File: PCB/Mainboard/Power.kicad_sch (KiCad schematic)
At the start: 17 parts, among them Q1 P-Channel, U4 TPS62177, U5 TPS2111

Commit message: Update schematic and lay-out
- Swap out CP2102N, ATmega328PB and CP with new Kicad 6 symbol
- Correct all links to point to new zoudio_symbols and zoudio_footprint libraries
- Lay-out updated, only antenna is left to update.
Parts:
- Q1: footprint ZOUDIO-footprints:SOIC8_mosfet -> zoudio_footprints:SOIC8_mosfet
- U4: footprint ZOUDIO-footprints:WSON-10-1EP_2x3mm_P0.5mm_EP0.84x2.4mm -> zoudio_footprints:WSON-10-1EP_2x3mm_P0.5mm_EP0.84x2.4mm
- U5: symbol ZOUDIO-symbols:TPS211xA -> zoudio_symbols:TPS211xA
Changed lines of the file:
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@@
       (effects (font (size 1.524 1.524)))
     )
-    (property "Footprint" "ZOUDIO-footprints:SOIC8_mosfet" (id 2) (at 87.63 128.27 0)
+    (property "Footprint" "zoudio_footprints:SOIC8_mosfet" (id 2) (at 87.63 128.27 0)
       (effects (font (size 1.524 1.524)) hide)
     )
@@
     (property "Reference" "U4" (id 0) (at 107.95 73.66 0))
     (property "Value" "TPS62177" (id 1) (at 107.95 76.2 0))
-    (property "Footprint" "ZOUDIO-footprints:WSON-10-1EP_2x3mm_P0.5mm_EP0.84x2.4mm" (id 2) (at 111.76 100.33 0)
+    (property "Footprint" "zoudio_footprints:WSON-10-1EP_2x3mm_P0.5mm_EP0.84x2.4mm" (id 2) (at 111.76 100.33 0)
       (effects (font (size 1.27 1.27)) (justify left) hide)
     )
@@
     (pin "1")
   )
-  (symbol (lib_id "ZOUDIO-symbols:TPS211xA") (at 196.85 88.9 0) (unit 1)
+  (symbol (lib_id "zoudio_symbols:TPS211xA") (at 196.85 88.9 0) (unit 1)
     (in_bom yes) (on_board yes)
     (property "Reference" "U5" (id 0) (at 196.85 81.28 0))

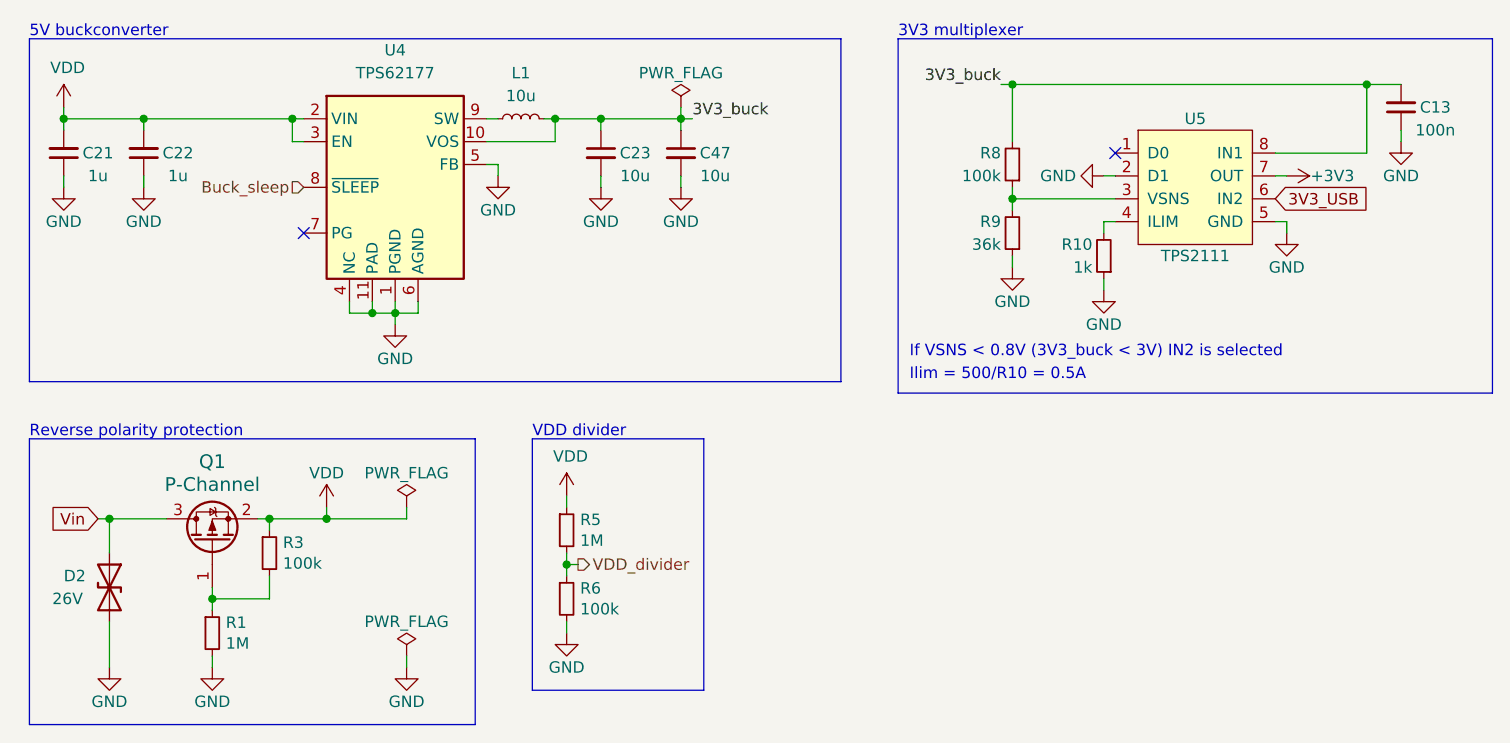
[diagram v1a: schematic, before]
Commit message: Add buck, change some part values
Add new buck in schematic and layout.
Modify BT module footprint,
Change power led resistor from 1k to 100R
Change 4.7u TAS resistors to 10u (consolidation)
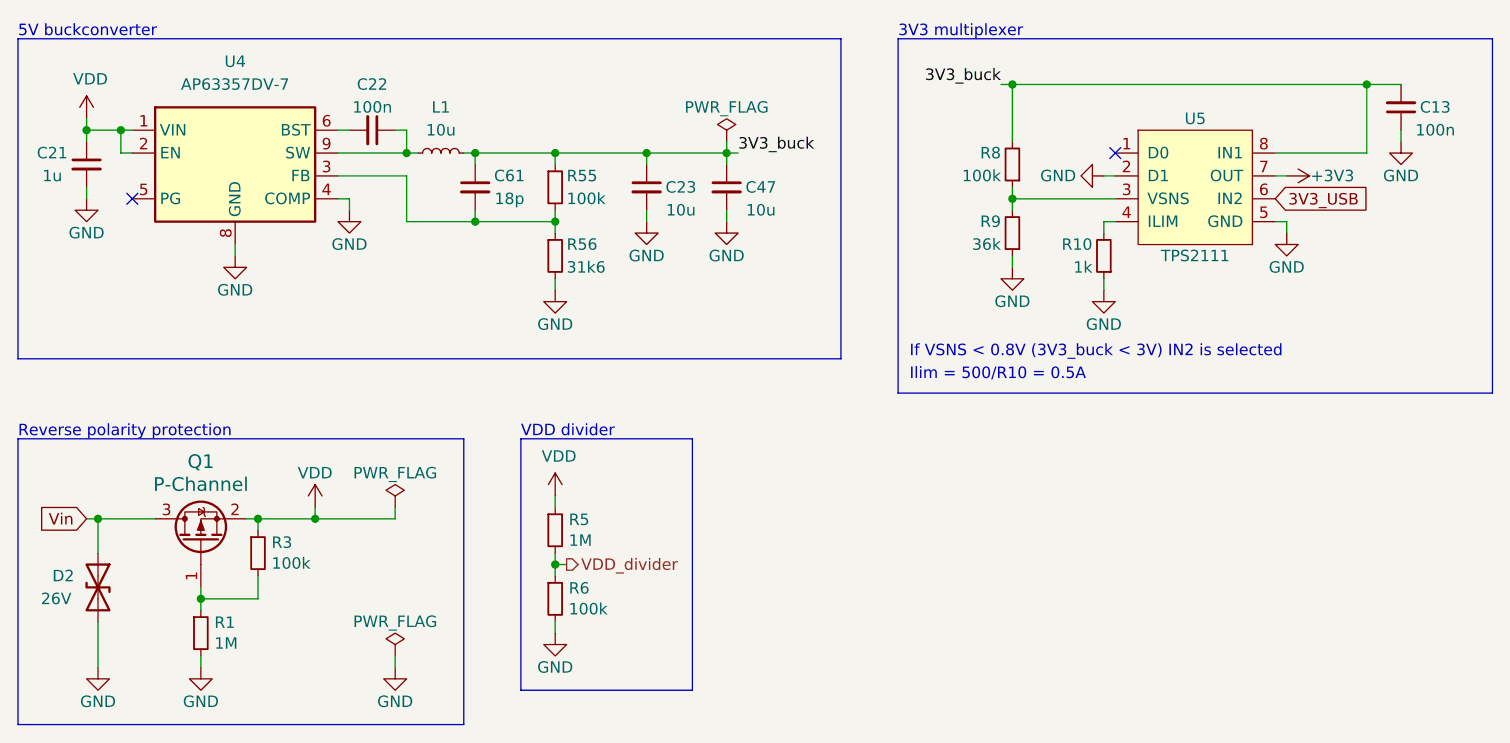
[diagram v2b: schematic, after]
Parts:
- removed U4: TPS62177, zoudio_footprints:WSON-10-1EP_2x3mm_P0.5mm_EP0.84x2.4mm, symbol Regulator_Switching:TPS62177DQC
- added C61: 18p, Capacitor_SMD:C_0603_1608Metric, symbol Device:C_Small
- added R55: 100k, Resistor_SMD:R_0603_1608Metric, symbol Device:R_Small
- added R56: 31k6, Resistor_SMD:R_0603_1608Metric, symbol Device:R_Small
- added U4: AP63357DV-7, zoudio_footprints:V-DFN3020-13, symbol zoudio_symbols:AP63357DV-7
- C22: value 1u -> 100n; footprint Capacitor_SMD:C_0805_2012Metric -> Capacitor_SMD:C_0603_1608Metric; Manufacturer Taiyo Yuden -> Murata; Partnumber UMK212B7105KG-T -> GCM188L81H104KA57D
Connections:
- net 3V3_buck: now also C61.1, R55.1
- net GND: now also C21.2, R56.2, U4.4 (COMP), U4.8 (GND); no longer C21.1, C22.1
- net VDD: now also C21.1, U4.1 (VIN), U4.2 (EN); no longer C21.2, C22.2
- net at L1.1: now also C22.1, U4.9 (SW)
- new net: C61.2, R55.2, R56.1, U4.3 (FB)
- new net: C22.2, U4.6 (BST)
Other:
- moved on the sheet: C23, C47, D2, L1, Q1, R1, R3, R5, R6

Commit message: Mainboard: update symbol fields for bom export
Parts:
- C61: Partnumber 0603B104J500CT -> C0603C180K8GACTU
- R55: Partnumber RC0603FR-071KL -> RC0603FR-07100KL
- R56: Partnumber RC0603FR-071KL -> RC0603FR-0731K6L
- U4: Manufacturer (none) -> Diodes Inc; Partnumber (none) -> AP63357DV-7
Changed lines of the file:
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@@
       (effects (font (size 1.27 1.27)) hide)
     )
-    (property "Partnumber" "RC0603FR-071KL" (id 5) (at 125.73 96.52 0)
+    (property "Partnumber" "RC0603FR-0731K6L" (id 5) (at 125.73 96.52 0)
       (effects (font (size 1.27 1.27)) hide)
     )
@@
     )
     (property "Datasheet" "" (id 3) (at 90.17 73.66 0)
+      (effects (font (size 1.27 1.27)) hide)
+    )
+    (property "Manufacturer" "Diodes Inc" (id 4) (at 90.17 87.63 0)
+      (effects (font (size 1.27 1.27)) hide)
+    )
+    (property "Partnumber" "AP63357DV-7" (id 5) (at 90.17 87.63 0)
       (effects (font (size 1.27 1.27)) hide)
     )
@@
       (effects (font (size 1.27 1.27)) hide)
     )
-    (property "Partnumber" "RC0603FR-071KL" (id 5) (at 125.73 88.9 0)
+    (property "Partnumber" "RC0603FR-07100KL" (id 5) (at 125.73 88.9 0)
       (effects (font (size 1.27 1.27)) hide)
     )
@@
       (effects (font (size 1.27 1.27)) hide)
     )
-    (property "Partnumber" "0603B104J500CT" (id 5) (at 116.84 88.9 0)
+    (property "Partnumber" "C0603C180K8GACTU" (id 5) (at 116.84 88.9 0)
       (effects (font (size 1.27 1.27)) hide)
     )

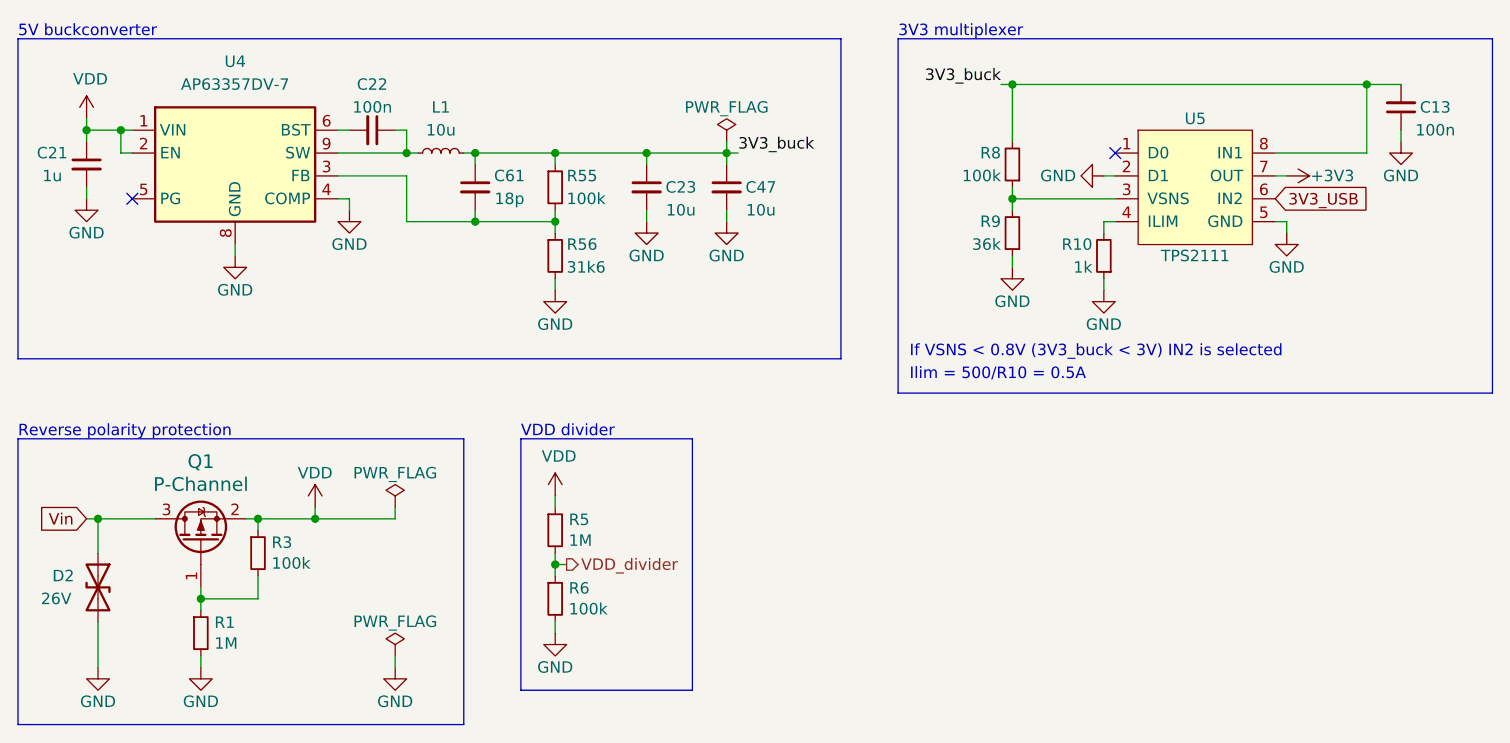
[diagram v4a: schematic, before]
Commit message: Mainboard: version 1.1.1
- No change in electrical connectivity
- Make 3D model more complete
- Improvements in paste layer for manufacturability
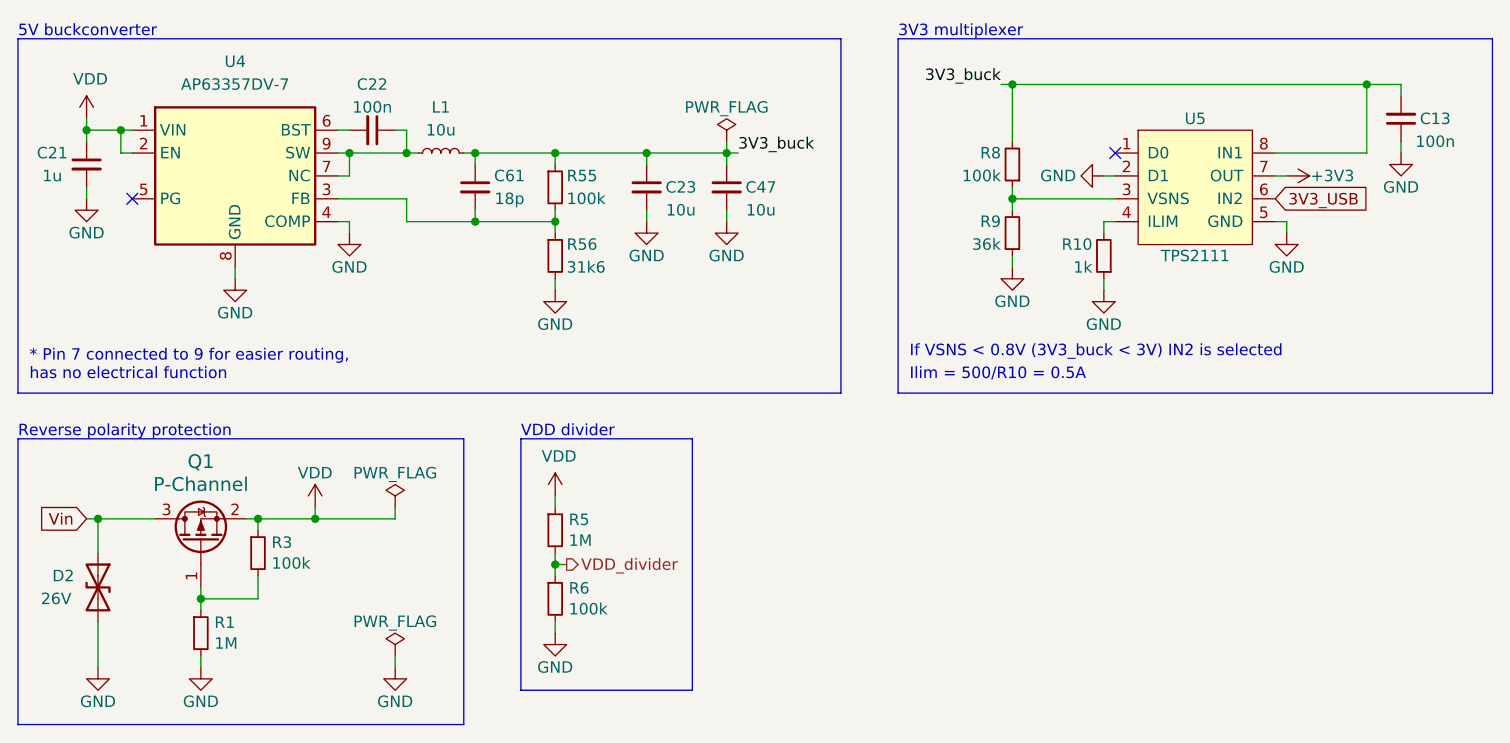
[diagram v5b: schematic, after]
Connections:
- net at C22.1, L1.1, U4.9 (SW): now also U4.7 (NC)
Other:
- note added: "* Pin 7 connected to 9 for easier routing, has no electrical function"
- moved on the sheet: C13
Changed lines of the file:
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@@
   (title_block
     (title "4x38W amp with DSP and BT")
-    (date "2022-02-12")
-    (rev "1.1")
+    (date "2022-04-17")
+    (rev "1.1.1")
     (company "ZOUDIO")
   )
@@
   )
   (junction (at 144.78 85.09) (diameter 0) (color 0 0 0 0)
+  )
+  (junction (at 102.87 85.09) (diameter 0) (color 0 0 0 0)
   )
   (junction (at 215.9 77.47) (diameter 0) (color 0 0 0 0)
@@
     (stroke (width 0) (type default) (color 0 0 0 0))
   )
+  (wire (pts (xy 102.87 87.63) (xy 102.87 85.09))
+    (stroke (width 0) (type default) (color 0 0 0 0))
+  )
   (wire (pts (xy 186.69 93.98) (xy 186.69 92.71))
     (stroke (width 0) (type default) (color 0 0 0 0))
@@
     (stroke (width 0) (type default) (color 0 0 0 0))
   )
+  (wire (pts (xy 101.6 87.63) (xy 102.87 87.63))
+    (stroke (width 0) (type default) (color 0 0 0 0))
+  )
   (wire (pts (xy 186.69 87.63) (xy 187.96 87.63))
     (stroke (width 0) (type default) (color 0 0 0 0))
@@
     (stroke (width 0) (type default) (color 0 0 0 0))
   )
-  (wire (pts (xy 109.22 87.63) (xy 109.22 92.71))
-    (stroke (width 0) (type default) (color 0 0 0 0))
-  )
   (wire (pts (xy 107.95 82.55) (xy 109.22 82.55))
     (stroke (width 0) (type default) (color 0 0 0 0))
@@
     (stroke (width 0) (type default) (color 0 0 0 0))
   )
-  (polyline (pts (xy 157.48 72.39) (xy 157.48 107.95))
+  (polyline (pts (xy 157.48 72.39) (xy 157.48 111.76))
+    (stroke (width 0) (type default) (color 0 0 0 0))
+  )
+  (wire (pts (xy 101.6 90.17) (xy 109.22 90.17))
     (stroke (width 0) (type default) (color 0 0 0 0))
   )
@@
     (stroke (width 0) (type default) (color 0 0 0 0))
   )
+  (wire (pts (xy 219.71 77.47) (xy 219.71 78.74))
+    (stroke (width 0) (type default) (color 0 0 0 0))
+  )
   (wire (pts (xy 77.47 82.55) (xy 77.47 85.09))
     (stroke (width 0) (type default) (color 0 0 0 0))
@@
     (stroke (width 0) (type default) (color 0 0 0 0))
   )
-  (polyline (pts (xy 157.48 107.95) (xy 66.04 107.95))
+  (polyline (pts (xy 157.48 111.76) (xy 66.04 111.76))
     (stroke (width 0) (type default) (color 0 0 0 0))
   )
@@
     (stroke (width 0) (type default) (color 0 0 0 0))
   )
-  (wire (pts (xy 102.87 90.17) (xy 101.6 90.17))
+  (wire (pts (xy 102.87 92.71) (xy 101.6 92.71))
     (stroke (width 0) (type default) (color 0 0 0 0))
   )
@@
     (stroke (width 0) (type default) (color 0 0 0 0))
   )
-  (wire (pts (xy 219.71 82.55) (xy 219.71 83.82))
+  (wire (pts (xy 219.71 83.82) (xy 219.71 85.09))
     (stroke (width 0) (type default) (color 0 0 0 0))
   )
@@
     (stroke (width 0) (type default) (color 0 0 0 0))
   )
-  (wire (pts (xy 90.17 95.25) (xy 90.17 96.52))
+  (wire (pts (xy 90.17 97.79) (xy 90.17 99.06))
     (stroke (width 0) (type default) (color 0 0 0 0))
   )
@@
     (stroke (width 0) (type default) (color 0 0 0 0))
   )
+  (wire (pts (xy 102.87 85.09) (xy 101.6 85.09))
+    (stroke (width 0) (type default) (color 0 0 0 0))
+  )
   (wire (pts (xy 116.84 86.36) (xy 116.84 85.09))
     (stroke (width 0) (type default) (color 0 0 0 0))
@@
     (stroke (width 0) (type default) (color 0 0 0 0))
   )
+  (wire (pts (xy 109.22 90.17) (xy 109.22 92.71))
+    (stroke (width 0) (type default) (color 0 0 0 0))
+  )
   (polyline (pts (xy 229.87 72.39) (xy 229.87 111.76))
     (stroke (width 0) (type default) (color 0 0 0 0))
@@
     (stroke (width 0) (type default) (color 0 0 0 0))
   )
-  (wire (pts (xy 109.22 85.09) (xy 101.6 85.09))
+  (wire (pts (xy 109.22 85.09) (xy 102.87 85.09))
     (stroke (width 0) (type default) (color 0 0 0 0))
   )
@@
     (stroke (width 0) (type default) (color 0 0 0 0))
   )
-  (wire (pts (xy 102.87 91.44) (xy 102.87 90.17))
+  (wire (pts (xy 102.87 93.98) (xy 102.87 92.71))
     (stroke (width 0) (type default) (color 0 0 0 0))
   )
@@
     (stroke (width 0) (type default) (color 0 0 0 0))
   )
-  (polyline (pts (xy 66.04 72.39) (xy 66.04 107.95))
+  (polyline (pts (xy 66.04 72.39) (xy 66.04 111.76))
     (stroke (width 0) (type default) (color 0 0 0 0))
   )
@@
   )
   (polyline (pts (xy 121.92 144.78) (xy 140.97 144.78))
-    (stroke (width 0) (type default) (color 0 0 0 0))
-  )
-  (wire (pts (xy 101.6 87.63) (xy 109.22 87.63))
     (stroke (width 0) (type default) (color 0 0 0 0))
   )
@@
   )
   (text "If VSNS < 0.8V (3V3_buck < 3V) IN2 is selected" (at 165.1 107.95 0)
+    (effects (font (size 1.27 1.27)) (justify left bottom))
+  )
+  (text "* Pin 7 connected to 9 for easier routing, \nhas no electrical function"
+    (at 67.31 110.49 0)
     (effects (font (size 1.27 1.27)) (justify left bottom))
   )
@@
     (pin "1")
   )
-  (symbol (lib_id "Device:C_Small") (at 219.71 80.01 180) (unit 1)
-    (in_bom yes) (on_board yes)
-    (property "Reference" "C13" (id 0) (at 223.52 80.01 0))
-    (property "Value" "100n" (id 1) (at 223.52 82.55 0))
-    (property "Footprint" "Capacitor_SMD:C_0603_1608Metric" (id 2) (at 219.71 80.01 0)
-      (effects (font (size 1.27 1.27)) hide)
-    )
-    (property "Datasheet" "~" (id 3) (at 219.71 80.01 0)
-      (effects (font (size 1.27 1.27)) hide)
-    )
-    (property "Manufacturer" "Murata" (id 4) (at 219.71 80.01 0)
-      (effects (font (size 1.27 1.27)) hide)
-    )
-    (property "Partnumber" "GCM188L81H104KA57D" (id 5) (at 219.71 80.01 0)
-      (effects (font (size 1.27 1.27)) hide)
-    )
-    (pin "1")
-    (pin "2")
-  )
-  (symbol (lib_id "power:GND") (at 219.71 83.82 0) (unit 1)
-    (in_bom yes) (on_board yes)
-    (property "Reference" "#PWR0139" (id 0) (at 219.71 90.17 0)
-      (effects (font (size 1.27 1.27)) hide)
-    )
-    (property "Value" "GND" (id 1) (at 219.71 87.63 0))
-    (property "Footprint" "" (id 2) (at 219.71 83.82 0)
-      (effects (font (size 1.27 1.27)) hide)
-    )
-    (property "Datasheet" "" (id 3) (at 219.71 83.82 0)
+  (symbol (lib_id "Device:C_Small") (at 219.71 81.28 180) (unit 1)
+    (in_bom yes) (on_board yes)
+    (property "Reference" "C13" (id 0) (at 223.52 81.28 0))
+    (property "Value" "100n" (id 1) (at 223.52 83.82 0))
+    (property "Footprint" "Capacitor_SMD:C_0603_1608Metric" (id 2) (at 219.71 81.28 0)
+      (effects (font (size 1.27 1.27)) hide)
+    )
+    (property "Datasheet" "~" (id 3) (at 219.71 81.28 0)
+      (effects (font (size 1.27 1.27)) hide)
+    )
+    (property "Manufacturer" "Murata" (id 4) (at 219.71 81.28 0)
+      (effects (font (size 1.27 1.27)) hide)
+    )
+    (property "Partnumber" "GCM188L81H104KA57D" (id 5) (at 219.71 81.28 0)
+      (effects (font (size 1.27 1.27)) hide)
+    )
+    (pin "1")
+    (pin "2")
+  )
+  (symbol (lib_id "power:GND") (at 219.71 85.09 0) (unit 1)
+    (in_bom yes) (on_board yes)
+    (property "Reference" "#PWR0139" (id 0) (at 219.71 91.44 0)
+      (effects (font (size 1.27 1.27)) hide)
+    )
+    (property "Value" "GND" (id 1) (at 219.71 88.9 0))
+    (property "Footprint" "" (id 2) (at 219.71 85.09 0)
+      (effects (font (size 1.27 1.27)) hide)
+    )
+    (property "Datasheet" "" (id 3) (at 219.71 85.09 0)
       (effects (font (size 1.27 1.27)) hide)
     )
@@
     (pin "2")
   )
-  (symbol (lib_id "power:GND") (at 102.87 91.44 0) (unit 1)
-    (in_bom yes) (on_board yes)
-    (property "Reference" "#PWR0129" (id 0) (at 102.87 97.79 0)
-      (effects (font (size 1.27 1.27)) hide)
-    )
-    (property "Value" "GND" (id 1) (at 102.87 95.25 0))
-    (property "Footprint" "" (id 2) (at 102.87 91.44 0)
-      (effects (font (size 1.27 1.27)) hide)
-    )
-    (property "Datasheet" "" (id 3) (at 102.87 91.44 0)
-      (effects (font (size 1.27 1.27)) hide)
-    )
-    (pin "1")
-  )
-  (symbol (lib_id "power:GND") (at 90.17 96.52 0) (unit 1)
-    (in_bom yes) (on_board yes)
-    (property "Reference" "#PWR0124" (id 0) (at 90.17 102.87 0)
-      (effects (font (size 1.27 1.27)) hide)
-    )
-    (property "Value" "GND" (id 1) (at 90.17 100.33 0))
-    (property "Footprint" "" (id 2) (at 90.17 96.52 0)
-      (effects (font (size 1.27 1.27)) hide)
-    )
-    (property "Datasheet" "" (id 3) (at 90.17 96.52 0)
+  (symbol (lib_id "power:GND") (at 102.87 93.98 0) (unit 1)
+    (in_bom yes) (on_board yes)
+    (property "Reference" "#PWR0129" (id 0) (at 102.87 100.33 0)
+      (effects (font (size 1.27 1.27)) hide)
+    )
+    (property "Value" "GND" (id 1) (at 102.87 97.79 0))
+    (property "Footprint" "" (id 2) (at 102.87 93.98 0)
+      (effects (font (size 1.27 1.27)) hide)
+    )
+    (property "Datasheet" "" (id 3) (at 102.87 93.98 0)
+      (effects (font (size 1.27 1.27)) hide)
+    )
+    (pin "1")
+  )
+  (symbol (lib_id "power:GND") (at 90.17 99.06 0) (unit 1)
+    (in_bom yes) (on_board yes)
+    (property "Reference" "#PWR0124" (id 0) (at 90.17 105.41 0)
+      (effects (font (size 1.27 1.27)) hide)
+    )
+    (property "Value" "GND" (id 1) (at 90.17 102.87 0))
+    (property "Footprint" "" (id 2) (at 90.17 99.06 0)
+      (effects (font (size 1.27 1.27)) hide)
+    )
+    (property "Datasheet" "" (id 3) (at 90.17 99.06 0)
       (effects (font (size 1.27 1.27)) hide)
     )
@@
     (pin "5")
     (pin "6")
+    (pin "7")
     (pin "8")
     (pin "9")
